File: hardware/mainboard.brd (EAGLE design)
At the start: 116.8 x 77.2 mm, 171 parts, among them J1 AVR_SPI_PROG_3X2TESTPOINTS, J13 AVR_SPI_PROG_3X2TESTPOINTS, Q1 220mA/50V/3.5Ω, Q2 220mA/50V/3.5Ω, Q3 220mA/50V/3.5Ω, Q4 220mA/50V/3.5Ω, Q5 220mA/50V/3.5Ω, Q6 220mA/50V/3.5Ω, U1 ATTINY861V-10MU, U2 ATTINY861V-10MU

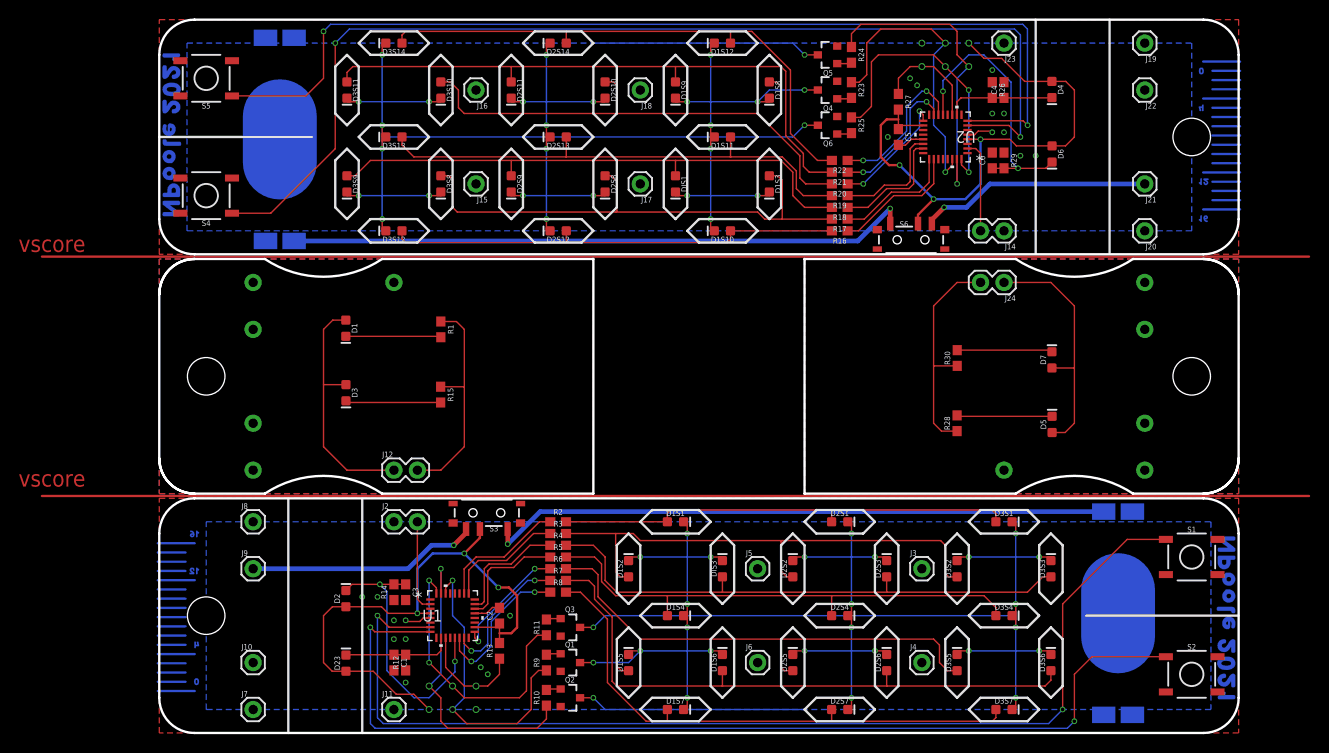
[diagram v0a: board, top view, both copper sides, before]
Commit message: Housekeeping
- Remove prototypes
- Remove EAGLE backup files
- Archive GHPages site
- Commit 3D CAD
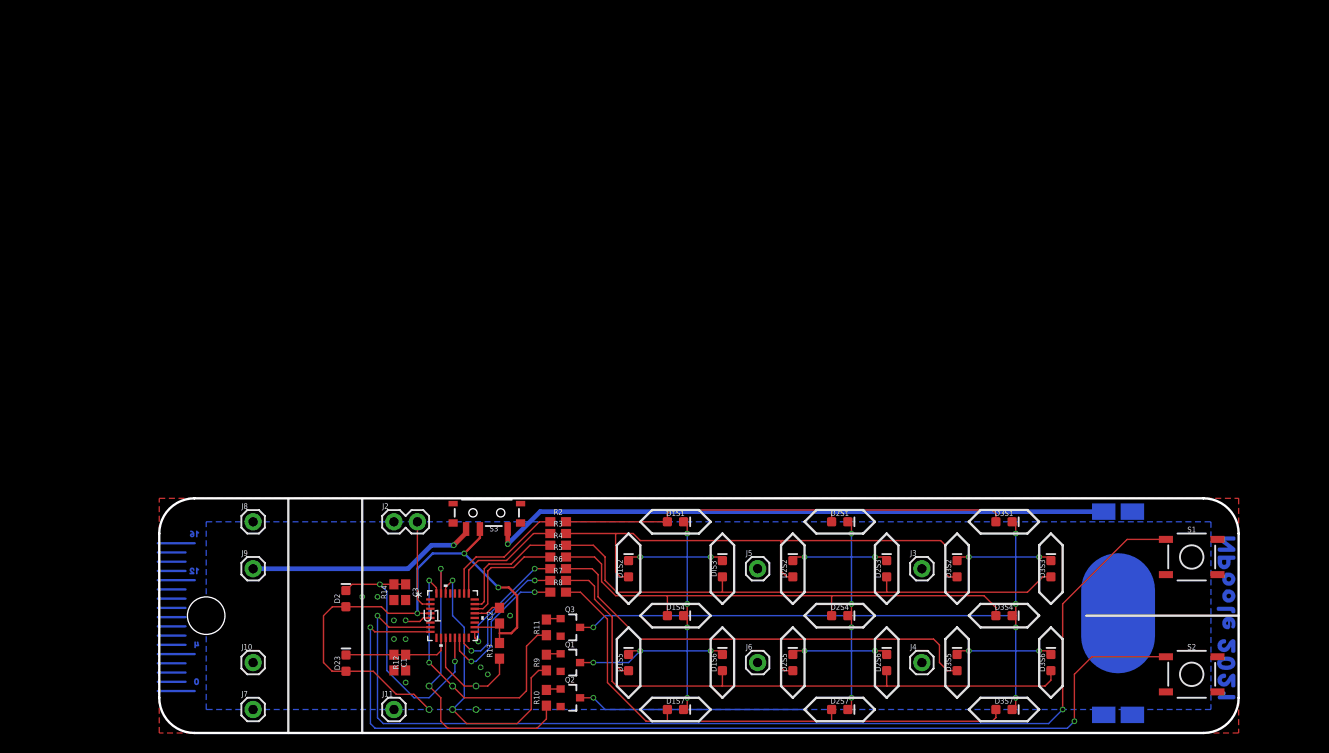
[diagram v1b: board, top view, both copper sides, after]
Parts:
- removed BT2: (no value), SparkFun-Batteries:BATTCON_20MM_4LEGS_OVERPASTE_INNER
- removed C4, C5, C6: 0.1uF, SparkFun-Capacitors:0603
- removed D1, D3, D5, D7: IR LED, SparkFun-LED:LED-0603
- removed D1S10, D1S11, D1S12, D1S3, D1S8, D1S9, D2S10, D2S11, D2S12, D2S13, D2S14, D2S8, D2S9, D3S10, D3S11, D3S12, D3S13, D3S14, D3S8, D3S9, DIS1: (no value), SparkFun-LED:LED-0603
- removed D4, D6: IR PHOTOTRANS, SparkFun-LED:LED-0603
- removed FRAME1: FRAME-LETTER, SparkFun-Aesthetics:CREATIVE_COMMONS
- removed J12, J14, J24: (no value), SparkFun-Connectors:1X02
- removed J13: AVR_SPI_PROG_3X2TESTPOINTS, SparkFun-Connectors:2X3_TEST_POINTS
- removed J15, J16, J17, J18, J19, J20, J21, J22, J23: (no value), SparkFun-Connectors:1X01
- removed Q4, Q5, Q6: 220mA/50V/3.5Ω, SparkFun-DiscreteSemi:SOT23-3
- removed R1, R15, R23, R24, R25, R26, R27, R28, R29, R30: 1k, SparkFun-Resistors:0603
- removed R16, R17, R18, R19, R20, R21, R22: 33, SparkFun-Resistors:0603
- removed S4, S5: MOMENTARY-SWITCH-SPST-SMD-5.2MM-TALL, SparkFun-Switches:TACTILE_SWITCH_SMD_5.2MM
- removed S6: (no value), SparkFun-Switches:SWITCH_SPST_SMD_A
- removed U$1, U$4: (no value), logo:LOGO#SVG0
- removed U$16: (no value), output:#PAUSE#CONTINUE_COUNTING#0
- removed U$2: (no value), output:#_3V#0
- removed U$27: (no value), output:#RESET_COUNTER#0
- removed U$28: (no value), output:#CHANGE_COMPONENT_PITCH#0
- removed U$29: (no value), output:QUICK#PRESS_THE_COUNT#RESET_BUTTON_TO_STOP_COUNTING0
- removed U$3: (no value), output:#_GND#0
- removed U$30: (no value), output:QUICK#PRESS_AGAIN_TO_RESUME0
- removed U$31: (no value), output:PRESS_AND_HOLD_THE_COUNT#RESET_BUTTON_UNTIL_THE0
- removed U$32: (no value), output:DISPLAY_BEGINS_BLINKING_THEN_RELEASE_TO_CLEAR_THE_CURRENT_COUNT0
- removed U$33: (no value), output:QUICK#PRESS_THE_SETUP_BUTTON_TO_DISPLAY_THE_COMPONENT_PITCH_IN_MM0
- removed U$34: (no value), output:PRESS_THE_SETUP_AGAIN_TO_EXIT_THE_PITCH_MENU0
- removed U$35: (no value), output:#GITHUB#COM#NPOOLE#BEANCOUNTER#0
- removed U$36: (no value), SparkFun-Aesthetics:OSHW-LOGO-M
- removed U$37: (no value), output:00
- removed U$38: (no value), output:40
- removed U$39: (no value), output:120
- removed U$40: (no value), output:160
- removed U$41: (no value), output:#ON#0
- removed U$42: (no value), output:#OFF#EXT#0
- removed U$43: (no value), output:NPOOLE_20210
- removed U$44: (no value), output:PRESS_THE_COUNT#RESET_BUTTON_TO_CHANGE_THE_PITCH_SETTING0
- removed U2: ATTINY861V-10MU, Melodica:32M1-A_ATM
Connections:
- removed net !RESET1: J13.5, R27.1, U2.11
- removed net 10: R19.1, U2.22
- removed net 10/SCK1: J13.3, R25.1, U2.32
- removed net 14: R20.1, U2.17
- removed net 15: R21.1, U2.15
- removed net 16: R22.1, U2.14
- removed net 17: J14.2, U2.2
- removed net 18: S4.1, U2.7
- removed net 19: S5.1, U2.8
- removed net 7: R16.1, U2.26
- removed net 8: R17.1, U2.25
- removed net 8/COPI1: J13.4, R23.1, U2.30
- removed net 9: R18.1, U2.23
- removed net 9/CIPO1: J13.1, R24.1, U2.31
- removed net GND1: BT2.2, C4.2, C5.2, C6.2, J13.6, J14.1, J22.1, Q4.2, Q5.2, Q6.2, R26.1, R29.1, S4.3, S5.3, U2.21, U2.5
- removed net IR_DETECTOR_A1: C4.1, D4.C, R26.2, U2.10
- removed net IR_DETECTOR_B1: C6.1, D6.C, R29.2, U2.13
- removed net N$19: Q4.1, R23.2
- removed net N$20: D1S10.C, D1S11.C, D1S12.C, D1S3.C, D1S8.C, D1S9.C, DIS1.C, Q4.3
- removed net N$21: D2S10.C, D2S11.C, D2S12.C, D2S13.C, D2S14.C, D2S8.C, D2S9.C, Q5.3
- removed net N$22: D3S10.C, D3S11.C, D3S12.C, D3S13.C, D3S14.C, D3S8.C, D3S9.C, Q6.3
- removed net N$23: Q5.1, R24.2
- removed net N$24: Q6.1, R25.2
- removed net N$30: BT2.1, S6.3
- removed net N$44: J12.2, R1.1, R15.1
- removed net N$45: D1.C, R1.2
- removed net N$46: D3.C, R15.2
- removed net N$51: D1.A, D3.A, J12.1
- removed net N$63: J24.2, R28.1, R30.1
- removed net N$64: D5.C, R28.2
- removed net N$65: D7.C, R30.2
- removed net N$66: D5.A, D7.A, J24.1
- removed net SEG10: D1S3.A, D2S8.A, D3S8.A, R17.2
- removed net SEG11: D2S9.A, D3S9.A, DIS1.A, R18.2
- removed net SEG12: D1S9.A, D2S11.A, D3S11.A, R21.2
- removed net SEG13: D1S8.A, D2S10.A, D3S10.A, R20.2
- removed net SEG14: D1S12.A, D2S14.A, D3S14.A, R22.2
- removed net SEG8: D1S10.A, D2S12.A, D3S12.A, R16.2
- removed net SEG9: D1S11.A, D2S13.A, D3S13.A, R19.2
- removed net V_BATT1: C5.1, D4.A, D6.A, J13.2, R27.2, S6.2, U2.18, U2.4
- removed net V_EXT1: J21.1, S6.1
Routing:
- net S$2: track 137.2 -> 0.00 mm
- net S$1: track 137.2 -> 0.00 mm
- net 18: track 117.9 -> 0.00 mm, vias 2 -> 0
- net 19: track 109.6 -> 0.00 mm, vias 2 -> 0
- net N$22: track 93.8 -> 0.00 mm, vias 9 -> 0
- net N$21: track 74.0 -> 0.00 mm, vias 9 -> 0
- net N$30: track 67.6 -> 0.00 mm, vias 1 -> 0
- net SEG12: track 66.8 -> 0.00 mm
- net V_BATT1: track 63.0 -> 0.00 mm, vias 3 -> 0
- net SEG11: track 60.1 -> 0.00 mm
- net SEG13: track 60.1 -> 0.00 mm
- net SEG14: track 59.9 -> 0.00 mm
- net SEG10: track 56.7 -> 0.00 mm
- net SEG9: track 55.1 -> 0.00 mm
- net N$20: track 50.6 -> 0.00 mm, vias 9 -> 0
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- removed copper zone on layer 1, net GND1
- removed copper zone on layer 16, net GND1
- removed copper zone on layer 16, net TAB1
- removed copper zone on layer 1, net TAB2
- removed copper zone on layer 16, net TAB5
- removed copper zone on layer 1, net TAB6
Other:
- board size 116.8 x 77.2 mm -> 116.8 x 25.4 mm
- board text removed: "NPOOLE"
- board text removed: "vscore"
